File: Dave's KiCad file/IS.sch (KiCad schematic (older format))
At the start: 0 parts

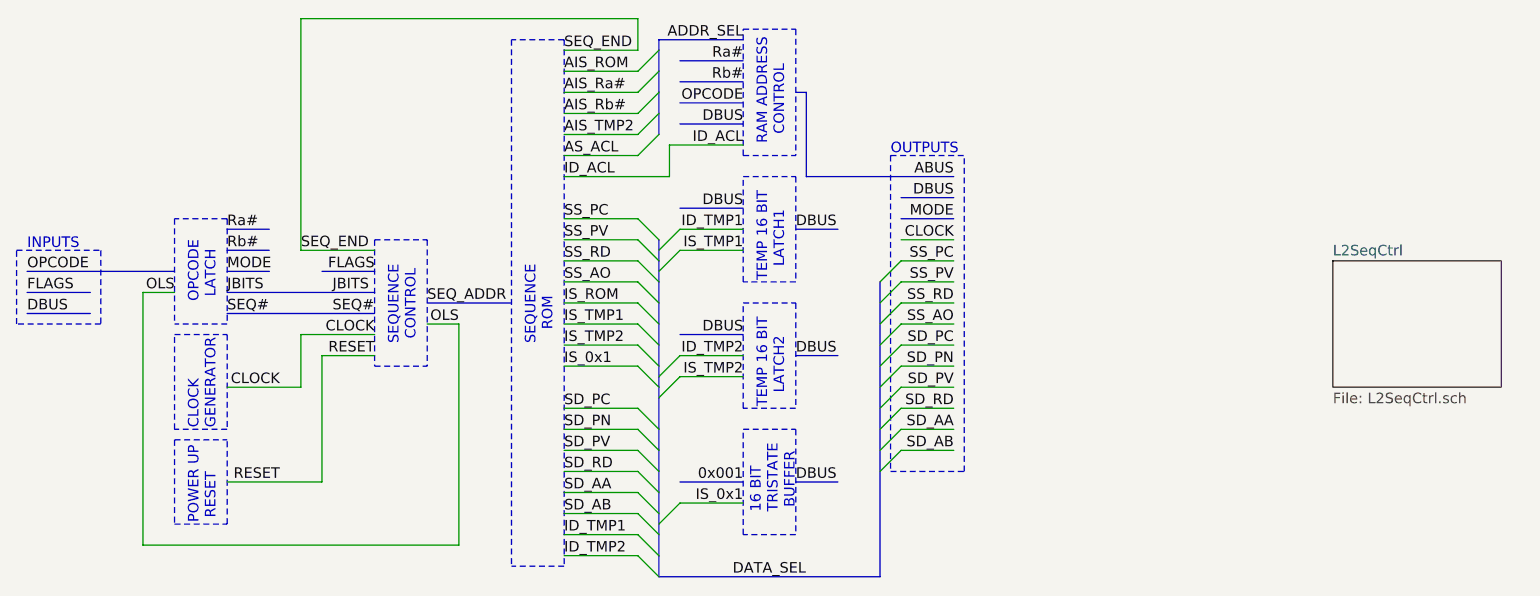
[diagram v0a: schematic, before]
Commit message: Add RESET to OUTPUTS
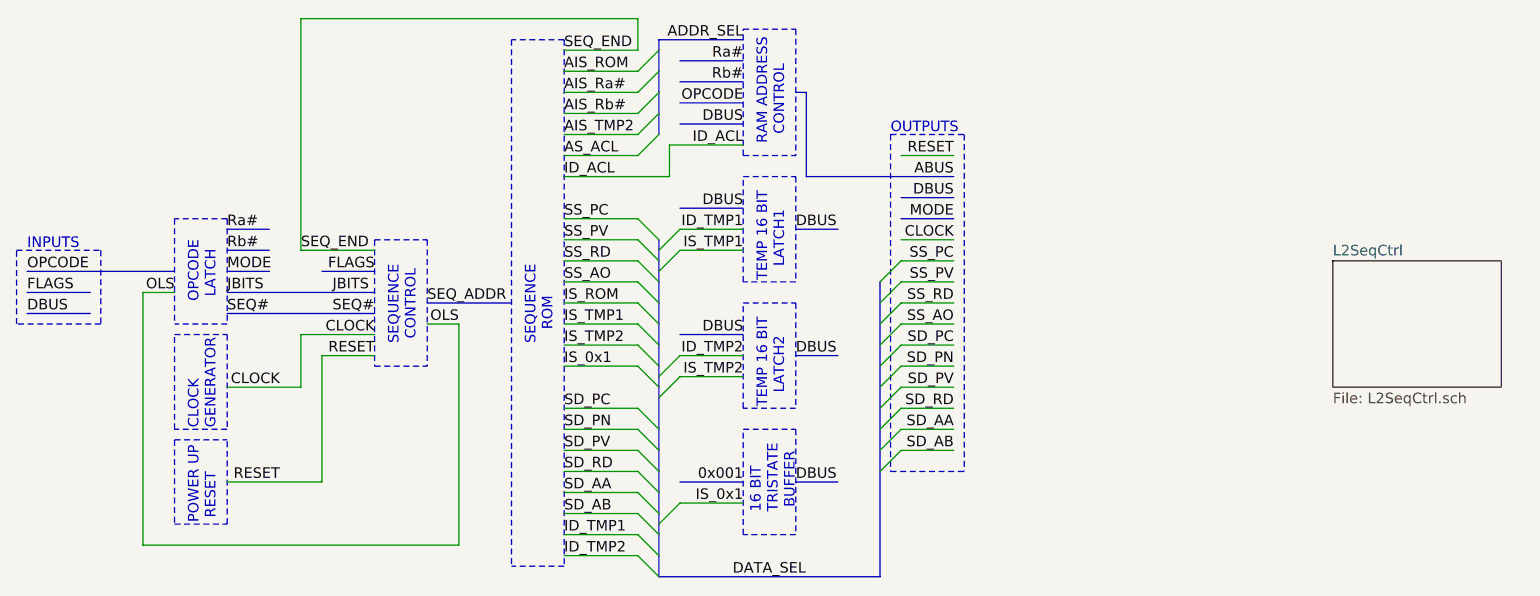
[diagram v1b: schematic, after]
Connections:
- wire segments 56 -> 57
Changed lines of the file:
@@
 Wire Notes Line style solid rgb(0, 255, 0)
 	5000 3350 4750 3350
-Wire Notes Line
-	5450 2750 5800 2750
 Text Label 5750 2950 2    50   ~ 0
 DBUS
@@
 Entry Wire Line
 	5400 3350 5500 3250
-Text Notes 5450 2750 0    50   ~ 0
+Text Notes 5450 2650 0    50   ~ 0
 OUTPUTS
 Text Label 5750 3050 2    50   ~ 0
@@
 Wire Notes Line
 	5450 4250 5800 4250
-Wire Notes Line
-	5450 2750 5450 4250
-Wire Notes Line
-	5800 4250 5800 2750
+Wire Wire Line
+	5500 2750 5750 2750
+Text Label 5750 2750 2    50   ~ 0
+RESET
+Wire Notes Line
+	5450 2650 5800 2650
+Wire Notes Line
+	5450 2650 5450 4250
+Wire Notes Line
+	5800 2650 5800 4250
 Wire Bus Line
 	4350 2200 4350 2650
